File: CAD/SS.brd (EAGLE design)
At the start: 77 x 99.7 mm, 117 parts, among them Q1 SN74AHC-NOR, Q2 UMD5N, Q4 SN74AHC-AND, Q5 BFP460, Q6 TCR1HF50, Q7 NCP553, T1 MMBTRA104SS, X1 ANTENNA, X2 RADIO, X3 INP, X4 AMP-O, X5 BPF-O

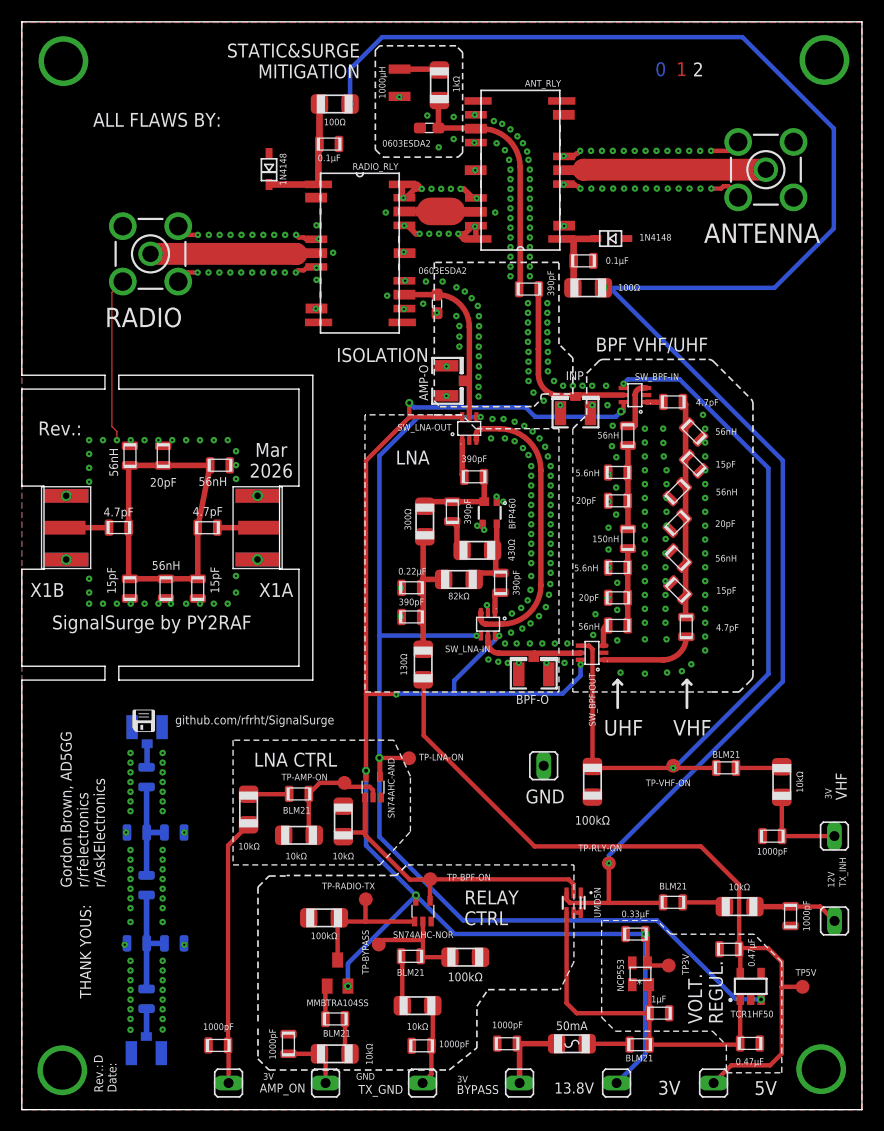
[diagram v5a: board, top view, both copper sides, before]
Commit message: Launching: Rev. E
* Complete rewrite of VHF BPF to a proper 3-pole ¤
* Improved UHF filter performance significantly¤
* Implemented a proper 50 ohm GCPW setup ¤
* Re-added soldermask into the signal path ¤
* Added a two-pole and three-pole test pad at the back of the board
* Fixed u.FL connectors lacking connection to ground in one side
* Added keep-out zones for RF inductors ¤
* Replaced the 3V regulator with one that can withstand the Vin ¤
* Separated the top ground plane on north/south: The north (RF) section
  doesn't have any thermal relief in GND pads. The south (ancillary)
  section contains thermal relief GND pads. ¤
* Fixed wrong limiters & pulldowns across the board ¤

All issues marked with ¤ were suggested by Gemini AI.
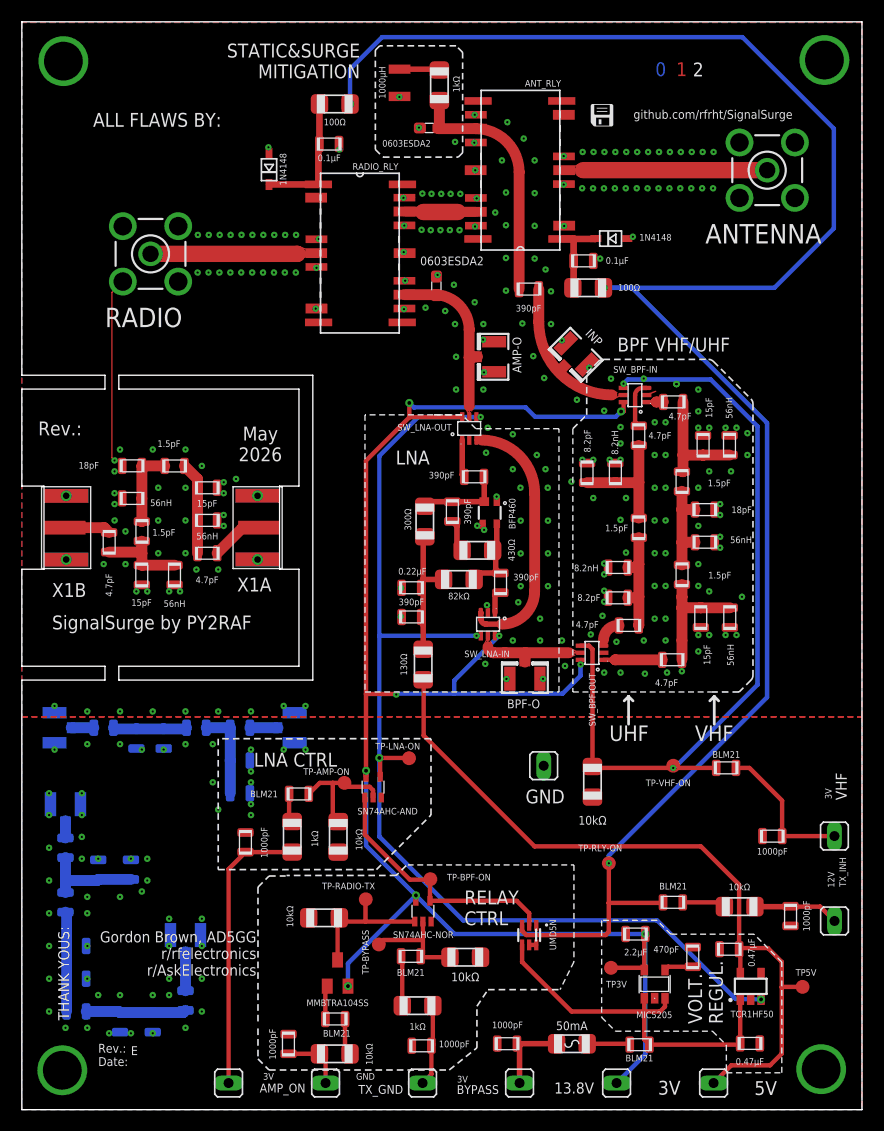
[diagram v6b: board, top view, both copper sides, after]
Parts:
- removed Q7: NCP553, aarf:SC-82AB
- removed R11, R16: 10kΩ, aarf:1206
- added C33, C35: 4.7pF, aarf:0805
- added C34, C36, C37, C38, C39: 1.5pF, aarf:0805
- added C40: Cin, aarf:0805
- added C41: Ct1, aarf:0805
- added C42: Cc1, aarf:0805
- added C43: Ct2, aarf:0805
- added C44: Cc2, aarf:0805
- added C45: Ct3, aarf:0805
- added C46: Cout, aarf:0805
- added Q3: MIC5205, aarf:SOT23-5
- added X3A, X3B: (no value), adafruit:U.FL
- C23: value 1µF -> 470pF
- C24: value 0.33µF -> 2.2µF
- C28, C3: value 20pF -> 18pF
- C31: value 20pF -> Ct1
- C32: value 20pF -> Ct2
- C6, C7: value 20pF -> 8.2pF
- L10, L11: value 5.6nH -> 8.2nH
- L13: value 150nH -> Cc
- L14: value 56nH -> Cout
- L15: value 56nH -> Cin
- L16: value 5.6nH -> L1
- L17: value 5.6nH -> L2
- L6: value 56nH -> Lt1
- L8: value 150nH -> Lt2
- L9: value 56nH -> Lt3
- R12, R7: value 10kΩ -> 1kΩ
- R13, R14, R17: value 100kΩ -> 10kΩ
- moved L9 69.2 mm to (12.0, 8.00), flipped to the bottom
- moved L8 64.7 mm to (5.00, 12.0), flipped to the bottom, turned to 180 degrees
- moved L6 49.9 mm to (10.0, 22.0), flipped to the bottom, turned to 90 degrees
- moved X2A 31.0 mm to (3.00, 35.0), turned to 180 degrees
- moved L15 25.1 mm to (7.50, 35.0), turned to 180 degrees
- moved C31 18.8 mm to (13.0, 34.0), turned to 90 degrees
- moved C20 18.8 mm to (20.5, 24.5), turned to 270 degrees
- moved L16 18.8 mm to (10.5, 34.0), turned to 270 degrees
- moved L13 15.1 mm to (16.0, 35.0), turned to 180 degrees
- moved X2B 13.5 mm to (25.0, 35.0), turned to 0 degrees
- moved L12 11.7 mm to (14.0, 49.0), turned to 270 degrees
- moved C32 11.5 mm to (20.0, 32.0), turned to 0 degrees
- moved L14 9.69 mm to (20.0, 35.0), turned to 180 degrees
- moved C27 9.29 mm to (17.0, 57.0), turned to 0 degrees
- moved L5 8.61 mm to (10.1, 56.0), turned to 0 degrees
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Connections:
- net N$10 renamed T-V-P1
- net N$12 renamed T-V-IN
- net N$2 renamed T-V-OUT
- net N$5 renamed D-V-OUT
- net N$6 renamed D-V-IN
- net N$9 renamed T-V-P2
- removed net BPF_VHF: C1.P$1, C2.P$1, C3.P$1, C4.P$1, C5.P$1, L1.P$2, L2.P$2, L3.P$1
- removed net N$11: C7.P$2, L11.P$1, L6.P$1, L8.P$2
- removed net N$42: FB5.P$1, R11.1
- removed net N$8: C6.P$2, L10.P$1, L8.P$1, L9.P$2
- new net D-V-P1: C26.P$1, C27.P$1, C38.P$2, L4.P$2
- new net D-V-P2: C28.P$1, C38.P$1, C39.P$2, L5.P$2
- new net D-V-P3: C29.P$1, C30.P$1, C39.P$1, L12.P$1
- new net T-U-IN: C40.P$1, X3A.3
- new net T-U-OUT: C46.P$1, X3B.3
- new net T-U-P1: C40.P$2, C41.P$1, C42.P$1, L6.P$1
- new net T-U-P2: C42.P$2, C43.P$1, C44.P$1, L8.P$1
- new net T-U-P3: C44.P$2, C45.P$1, C46.P$2, L9.P$1
- new net UHF-P1: C33.P$2, C34.P$1, C6.P$2, L10.P$1
- new net UHF-P2: C34.P$2, C35.P$1, C7.P$2, L11.P$1
- new net VHF-P1: C1.P$1, C2.P$1, C36.P$2, L1.P$2
- new net VHF-P3: C37.P$1, C4.P$1, C5.P$1, L3.P$1
- new net VPF-P2: C3.P$1, C36.P$1, C37.P$2, L2.P$2
- net 13.8V: now also Q3.1, Q3.3; no longer C23.P$2, Q7.2
- net 3V: now also Q3.5; no longer Q7.3
- net AMP+BPF_OUT: now also D4.1; no longer D4.2
- net BPF_ON: no longer R16.1
- net GND: now also C41.P$2, C43.P$2, C45.P$2, D4.2, L6.P$2, L8.P$2, L9.P$2, Q3.2, X3.1, X3A.1, X3A.2, X3B.1, X3B.2, X4.1, X5.1; no longer D4.1, Q7.1, R16.2
- net N$4: now also C23.P$2, Q3.4; no longer C26.P$1, C27.P$1, C28.P$1, C29.P$1, C30.P$1, L12.P$1, L4.P$2, L5.P$2
- net UHF-IN: now also C33.P$1; no longer L9.P$1
- net UHF-OUT: now also C35.P$2; no longer L6.P$2
- net VHF_ON_IN: now also FB5.P$1; no longer R11.2
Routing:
- net N$4: track 34.6 -> 2.67 mm
- net GND: track 50.4 -> 22.4 mm, vias 393 -> 308
- net BPF_VHF: track 22.8 -> 0.00 mm
- net BPF_IN1: track 16.1 -> 0.00 mm
- net AMP+BPF_OUT: track 3.67 -> 16.3 mm
- net AMP+BPF_OUT1: track 12.4 -> 0.00 mm
- net BPF_IN: track 1.02 -> 12.5 mm
- net UHF-P1: track 0.00 -> 11.4 mm
- net VHF-P3: track 0.00 -> 11.3 mm
- net VHF-P1: track 0.00 -> 10.8 mm
- net UHF-P2: track 0.00 -> 10.3 mm
- net T-U-P1: track 0.00 -> 9.24 mm
- net T-U-P3: track 0.00 -> 9.22 mm
- net VPF-P2: track 0.00 -> 9.14 mm
- net T-U-P2: track 0.00 -> 9.14 mm
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- added copper zone on layer 1, net AMP+BPF_OUT
- added copper zone on layer 1, net ANTENNA
- added copper zone on layer 1, net BPF_IN
- added copper zone on layer 1, net BPF_OUT
- added copper zone on layer 1, net RADIO
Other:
- board text added: "2-pole"
- board text added: "3-pole"
- board text added: "May 2026"
- board text removed: "ISOLATION"
- board text removed: "Mar 2026"
- board text removed: "UHF TEST BPF"

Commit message: Rev. E bug fixes
* Added new VHF filter test figures
* Fixed a gross error where a via shorted the VHF BPF final coupling stage
* Removed ground pad on inductors at the detachable VHF BPF.
* Improved the radio signal trace at the first RF relay input.
* Updated component values for the 3-pole VHF filter (*in vivo* performed differently than the *in vitro*)
* Updated BOM
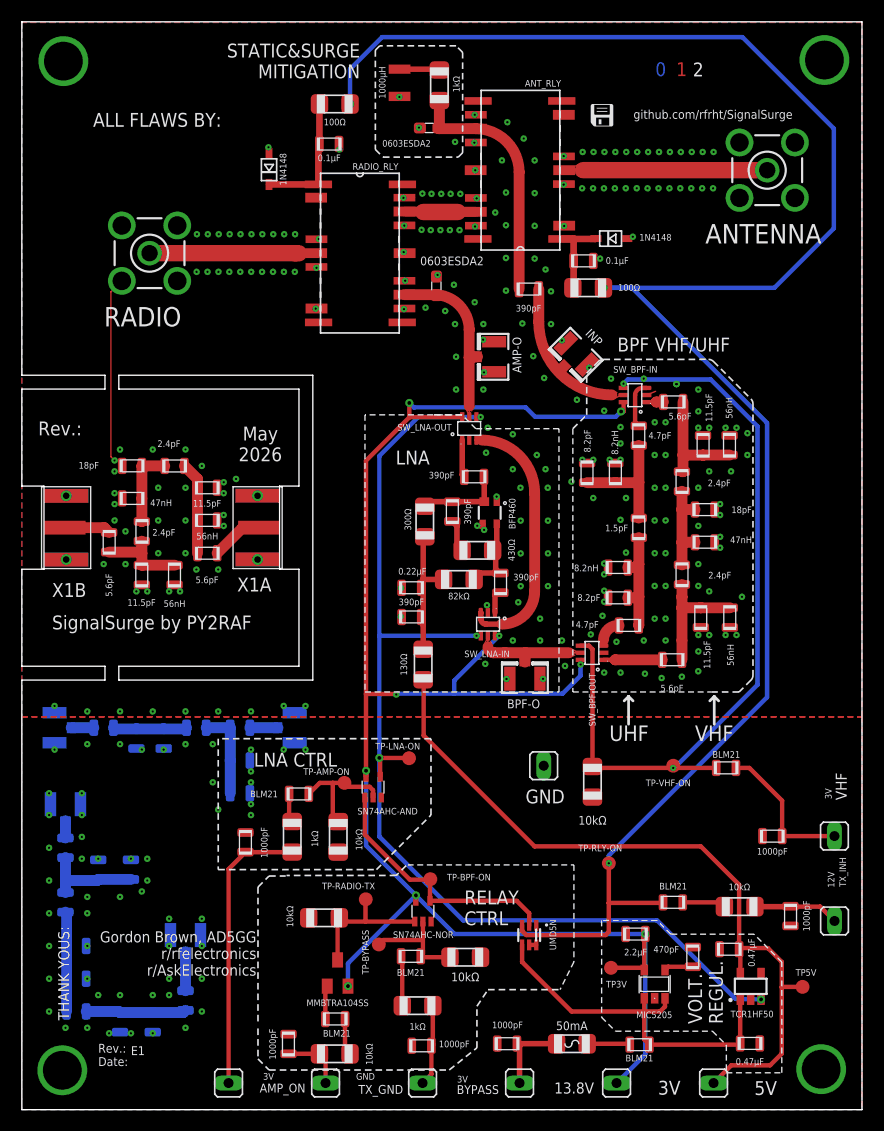
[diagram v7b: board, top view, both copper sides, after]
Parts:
- C1, C26, C30, C5: value 4.7pF -> 5.6pF
- C2, C27, C29, C4: value 15pF -> 11.5pF
- C36, C37, C38, C39: value 1.5pF -> 2.4pF
- L2, L5: value 56nH -> 47nH
- moved X2 0.11 mm to (11.7, 78.5)
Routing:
- net RADIO: track 15.2 -> 13.8 mm
- net GND: track 22.4 -> 22.5 mm, vias 308 -> 309
- removed copper zone on layer 1, net RADIO

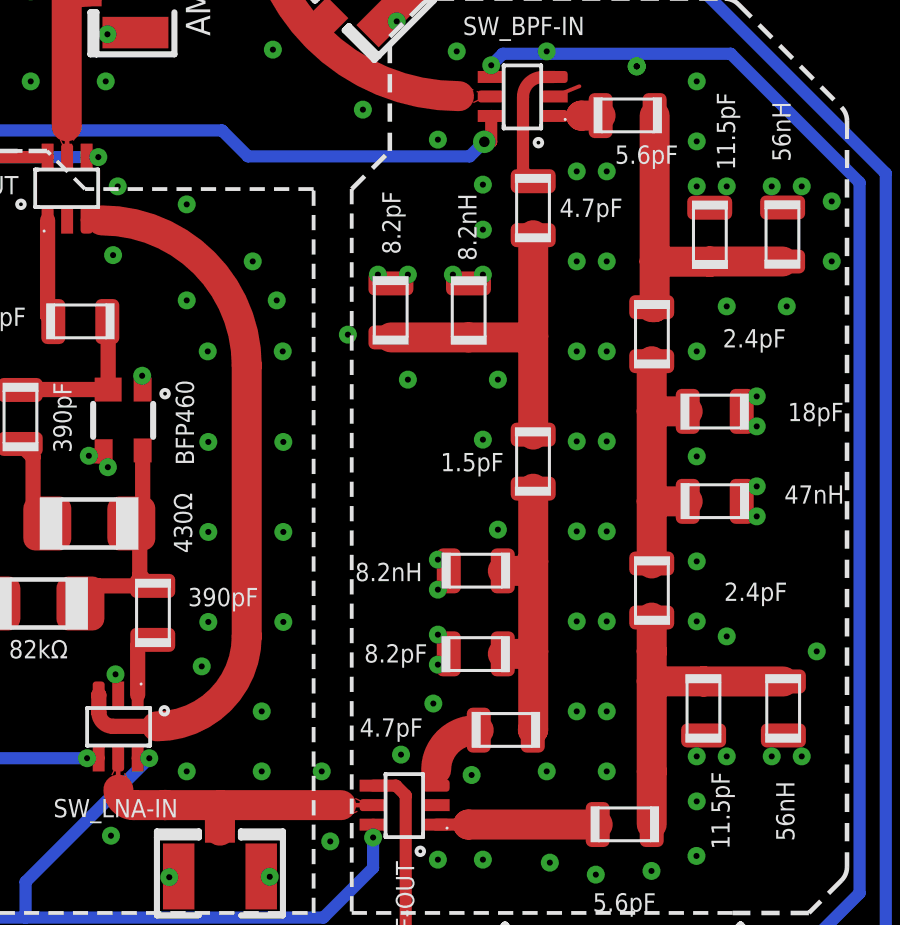
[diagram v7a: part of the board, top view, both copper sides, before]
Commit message: UHF filter improvements and testing figures.
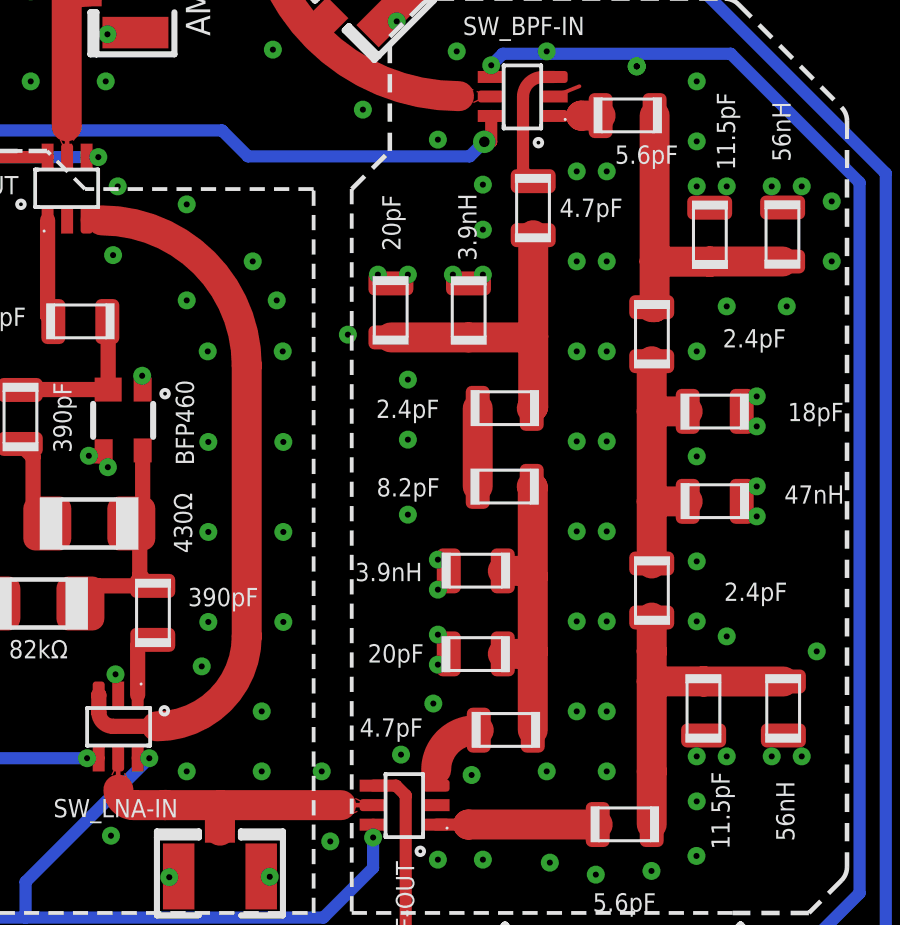
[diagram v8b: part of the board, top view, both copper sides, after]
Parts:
- added C47: 8.2pF, aarf:0805
- C34: value 1.5pF -> 2.4pF
- C6, C7: value 8.2pF -> 20pF
- L10, L11: value 8.2nH -> 3.9nH
- moved C34 2.01 mm to (55.6, 55.1), turned to 180 degrees
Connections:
- new net 1.86PF: C34.P$2, C47.P$1
- net UHF-P2: now also C47.P$2; no longer C34.P$2
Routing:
- net 1.86PF: track 0.00 -> 2.60 mm
- net UHF-P1: track 11.4 -> 10.6 mm
- net GND: vias 309 -> 308
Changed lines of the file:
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@@
 <setting verticaltext="up"/>
 </settings>
-<grid distance="0.5" unitdist="mm" unit="mm" style="lines" multiple="6" display="yes" altdistance="0.5" altunitdist="mil" altunit="mil"/>
+<grid distance="0.5" unitdist="mm" unit="mm" style="lines" multiple="6" display="yes" altdistance="0.1" altunitdist="mm" altunit="mm"/>
 <layers>
 <layer number="1" name="Top" color="4" fill="1" visible="yes" active="yes"/>
@@
 <attribute name="VALUE" x="56.256" y="14.441" size="0.6096" layer="21" font="vector" ratio="15" align="center"/>
 </element>
-<element name="C6" library="aarf" package="0805" value="8.2pF" x="51.806" y="58.3646" smashed="yes" rot="R270">
+<element name="C6" library="aarf" package="0805" value="20pF" x="51.806" y="58.3646" smashed="yes" rot="R270">
 <attribute name="VALUE" x="51.822" y="61.2856" size="0.6096" layer="21" font="vector" ratio="15" rot="R270" align="center"/>
 </element>
-<element name="C7" library="aarf" package="0805" value="8.2pF" x="54.6354" y="46.916" smashed="yes">
+<element name="C7" library="aarf" package="0805" value="20pF" x="54.6354" y="46.916" smashed="yes">
 <attribute name="VALUE" x="51.9684" y="46.932" size="0.6096" layer="21" font="vector" ratio="15" align="center"/>
 </element>
@@
 <attribute name="VALUE" x="51.8176" y="44.4626" size="0.6096" layer="21" font="vector" ratio="15" align="center"/>
 </element>
-<element name="C34" library="aarf" package="0805" value="1.5pF" x="56.5498" y="53.324" smashed="yes" rot="R270">
-<attribute name="VALUE" x="54.5138" y="53.309" size="0.6096" layer="21" font="vector" ratio="15" rot="R180" align="center"/>
+<element name="C34" library="aarf" package="0805" value="2.4pF" x="55.6" y="55.1" smashed="yes" rot="R180">
+<attribute name="VALUE" x="52.364" y="55.085" size="0.6096" layer="21" font="vector" ratio="15" rot="R180" align="center"/>
 </element>
 <element name="13.8V" library="aarf" package="JUMPER1" value="13.8V" x="45.62" y="2.44" smashed="yes" rot="R180">
@@
 <attribute name="VALUE" x="58.4804" y="61.7856" size="0.6096" layer="21" font="vector" ratio="15" rot="R180" align="center"/>
 </element>
-<element name="L10" library="aarf" package="0805" value="8.2nH" x="54.392" y="58.3646" smashed="yes" rot="R90">
+<element name="L10" library="aarf" package="0805" value="3.9nH" x="54.392" y="58.3646" smashed="yes" rot="R90">
 <attribute name="VALUE" x="54.354" y="61.1396" size="0.6096" layer="21" font="vector" ratio="15" rot="R90" align="center"/>
 </element>
-<element name="L11" library="aarf" package="0805" value="8.2nH" x="54.6354" y="49.683" smashed="yes" rot="R180">
+<element name="L11" library="aarf" package="0805" value="3.9nH" x="54.6354" y="49.683" smashed="yes" rot="R180">
 <attribute name="VALUE" x="51.7334" y="49.645" size="0.6096" layer="21" font="vector" ratio="15" rot="R180" align="center"/>
 </element>
@@
 <attribute name="VALUE" x="57.96" y="8.69" size="0.6096" layer="21" font="vector" ratio="15" align="center"/>
 </element>
+<element name="C47" library="aarf" package="0805" value="8.2pF" x="55.6" y="52.5" smashed="yes">
+<attribute name="VALUE" x="52.381" y="52.468" size="0.6096" layer="21" font="vector" ratio="15" align="center"/>
+</element>
 </elements>
 <signals>
@@
 <via x="53.372" y="49.058" extent="1-16" drill="0.2"/>
 <via x="53.372" y="50.058" extent="1-16" drill="0.2"/>
-<via x="55.372" y="51.058" extent="1-16" drill="0.2"/>
-<via x="54.872" y="54.058" extent="1-16" drill="0.2"/>
-<via x="55.372" y="56.058" extent="1-16" drill="0.2"/>
+<via x="52.372" y="51.558" extent="1-16" drill="0.2"/>
+<via x="52.372" y="54.058" extent="1-16" drill="0.2"/>
 <via x="52.372" y="56.058" extent="1-16" drill="0.2"/>
 <via x="50.372" y="57.558" extent="1-16" drill="0.2"/>
@@
 <signal name="UHF-P1" class="1">
 <contactref element="C33" pad="P$2"/>
-<contactref element="C34" pad="P$1"/>
 <contactref element="C6" pad="P$2"/>
 <contactref element="L10" pad="P$1"/>
-<wire x1="56.5498" y1="60.8728" x2="56.5498" y2="57.5056" width="1" layer="1"/>
-<wire x1="56.5498" y1="57.5056" x2="56.5498" y2="54.224" width="1" layer="1"/>
 <wire x1="51.806" y1="57.4646" x2="54.392" y2="57.4646" width="1" layer="1"/>
-<wire x1="54.392" y1="57.4646" x2="56.5088" y2="57.4646" width="1" layer="1"/>
-<wire x1="56.5088" y1="57.4646" x2="56.5498" y2="57.5056" width="1" layer="1"/>
+<contactref element="C34" pad="P$1"/>
+<wire x1="56.5498" y1="60.8728" x2="56.5498" y2="57.5" width="1" layer="1"/>
+<wire x1="56.5498" y1="57.5" x2="56.5498" y2="55.1498" width="1" layer="1"/>
+<wire x1="56.5498" y1="55.1498" x2="56.5" y2="55.1" width="1" layer="1"/>
+<wire x1="54.392" y1="57.4646" x2="56.5144" y2="57.4646" width="1" layer="1"/>
+<wire x1="56.5144" y1="57.4646" x2="56.5498" y2="57.5" width="1" layer="1"/>
 </signal>
 <signal name="UHF-P2" class="1">
-<contactref element="C34" pad="P$2"/>
 <contactref element="C35" pad="P$1"/>
 <contactref element="C7" pad="P$2"/>
 <contactref element="L11" pad="P$1"/>
-<wire x1="56.5498" y1="52.424" x2="56.5498" y2="50" width="1" layer="1"/>
-<wire x1="56.5498" y1="50" x2="56.5498" y2="47" width="1" layer="1"/>
-<wire x1="56.5498" y1="47" x2="56.5498" y2="44.3882" width="1" layer="1"/>
-<wire x1="56.5498" y1="44.3882" x2="56.5354" y2="44.3738" width="1" layer="1"/>
-<wire x1="55.5354" y1="49.683" x2="56.2328" y2="49.683" width="1" layer="1"/>
-<wire x1="56.2328" y1="49.683" x2="56.5498" y2="50" width="1" layer="1"/>
-<wire x1="55.5354" y1="46.916" x2="56.4658" y2="46.916" width="1" layer="1"/>
-<wire x1="56.4658" y1="46.916" x2="56.5498" y2="47" width="1" layer="1"/>
+<contactref element="C47" pad="P$2"/>
+<wire x1="56.5354" y1="44.3738" x2="56.5354" y2="47" width="1" layer="1"/>
+<wire x1="56.5354" y1="47" x2="56.5354" y2="49.5" width="1" layer="1"/>
+<wire x1="56.5354" y1="49.5" x2="56.5354" y2="52.4646" width="1" layer="1"/>
+<wire x1="56.5354" y1="52.4646" x2="56.5" y2="52.5" width="1" layer="1"/>
+<wire x1="55.5354" y1="46.916" x2="56.4514" y2="46.916" width="1" layer="1"/>
+<wire x1="56.4514" y1="46.916" x2="56.5354" y2="47" width="1" layer="1"/>
+<wire x1="55.5354" y1="49.683" x2="56.3524" y2="49.683" width="1" layer="1"/>
+<wire x1="56.3524" y1="49.683" x2="56.5354" y2="49.5" width="1" layer="1"/>
 </signal>
 <signal name="FEED-RB">
@@
 <wire x1="59.25" y1="13.1" x2="58.95" y2="12.8" width="0.4064" layer="1"/>
 </signal>
+<signal name="1.86PF" class="1">
+<contactref element="C34" pad="P$2"/>
+<contactref element="C47" pad="P$1"/>
+<wire x1="54.7" y1="52.5" x2="54.7" y2="55.1" width="1" layer="1"/>
+</signal>
 </signals>
